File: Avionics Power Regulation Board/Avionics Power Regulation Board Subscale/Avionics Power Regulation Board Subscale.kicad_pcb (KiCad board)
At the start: 2 copper layers, 7 parts, among them J1 282841-2, J2 282841-2, U1 LM2576HVS-5

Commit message: Updated Subscale Board
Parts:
- removed C1: EEUFR1V101B, EEUFR1V101B:CAPPRD350W60D800H1150
- removed C2: EEUTA1V102, EEUTA1V102:CAPPRD750W80D1600H2500
- removed D1: 1N5822, Diode_THT:D_DO-201AD_P15.24mm_Horizontal
- removed L1: RLB9012-101KL, RLB9012-101KL:IND_RLB9012-101KL
- added H1: MountingHole, MountingHole:MountingHole_2.1mm, F.Cu at (120.7, 105.4)
- added H3: MountingHole, MountingHole:MountingHole_2.1mm, F.Cu at (139.7, 54.6)
- added H4: MountingHole, MountingHole:MountingHole_2.1mm, F.Cu at (139.7, 77.5)
- added H5: MountingHole, MountingHole:MountingHole_2.1mm, F.Cu at (163.8, 54.6)
- added H6: MountingHole, MountingHole:MountingHole_2.1mm, F.Cu at (165.1, 77.5)
- added H7: MountingHole, MountingHole:MountingHole_2.1mm, F.Cu at (141.0, 105.4)
- J1: value 282841-2 -> Conn_01x04_Socket; footprint 282841-2:TE_282841-2 -> Connector_PinSocket_2.54mm:PinSocket_1x04_P2.54mm_Vertical
- J2: value 282841-2 -> Conn_01x06_Socket; footprint 282841-2:TE_282841-2 -> Connector_PinSocket_2.54mm:PinSocket_1x06_P2.54mm_Vertical
- U1: value LM2576HVS-5 -> SC0917; footprint Package_TO_SOT_SMD:TO-263-5_TabPin3 -> SC0917:MODULE_SC0917
- moved U1 142.5 mm to (211.6, 69.8), turned to 0 degrees
- moved J2 101.2 mm to (124.5, 118.1), turned to 90 degrees
- moved J1 88.0 mm to (139.7, 62.2), turned to 0 degrees
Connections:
- J1 pad 1: Net-(U1-FB) -> unconnected-(J1-Pin_1-Pad1)
- J1 pad 2: GNDREF -> unconnected-(J1-Pin_2-Pad2)
- J2 pad 1: GNDREF -> unconnected-(J2-Pin_1-Pad1)
- J2 pad 2: Net-(U1-VIN) -> unconnected-(J2-Pin_2-Pad2)
- U1 pad 1: Net-(U1-VIN) -> unconnected-(U1-GP0-Pad1)
- U1 pad 2: Net-(D1-K) -> unconnected-(U1-GP1-Pad2)
- U1 pad 4: Net-(U1-FB) -> unconnected-(U1-GP2-Pad4)
- U1 pad 5: GNDREF -> unconnected-(U1-GP3-Pad5)
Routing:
- net GNDREF: track 108.4 -> 0.00 mm
- net Net-(U1-VIN): track 41.4 -> 0.00 mm
- net Net-(U1-FB): track 40.1 -> 0.00 mm
- net Net-(D1-K): track 25.5 -> 0.00 mm
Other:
- board text added: "BMP 280"

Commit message: Updated Subscale Part 3
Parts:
- moved U1 12.4 mm to (224.0, 68.6)
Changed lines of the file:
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@@
 	(footprint "SC0917:MODULE_SC0917"
 		(layer "F.Cu")
-		(at 211.62 69.85)
+		(at 223.99 68.58)
 		(property "Reference" "U1"
 			(at -8.325 -28.635 0)

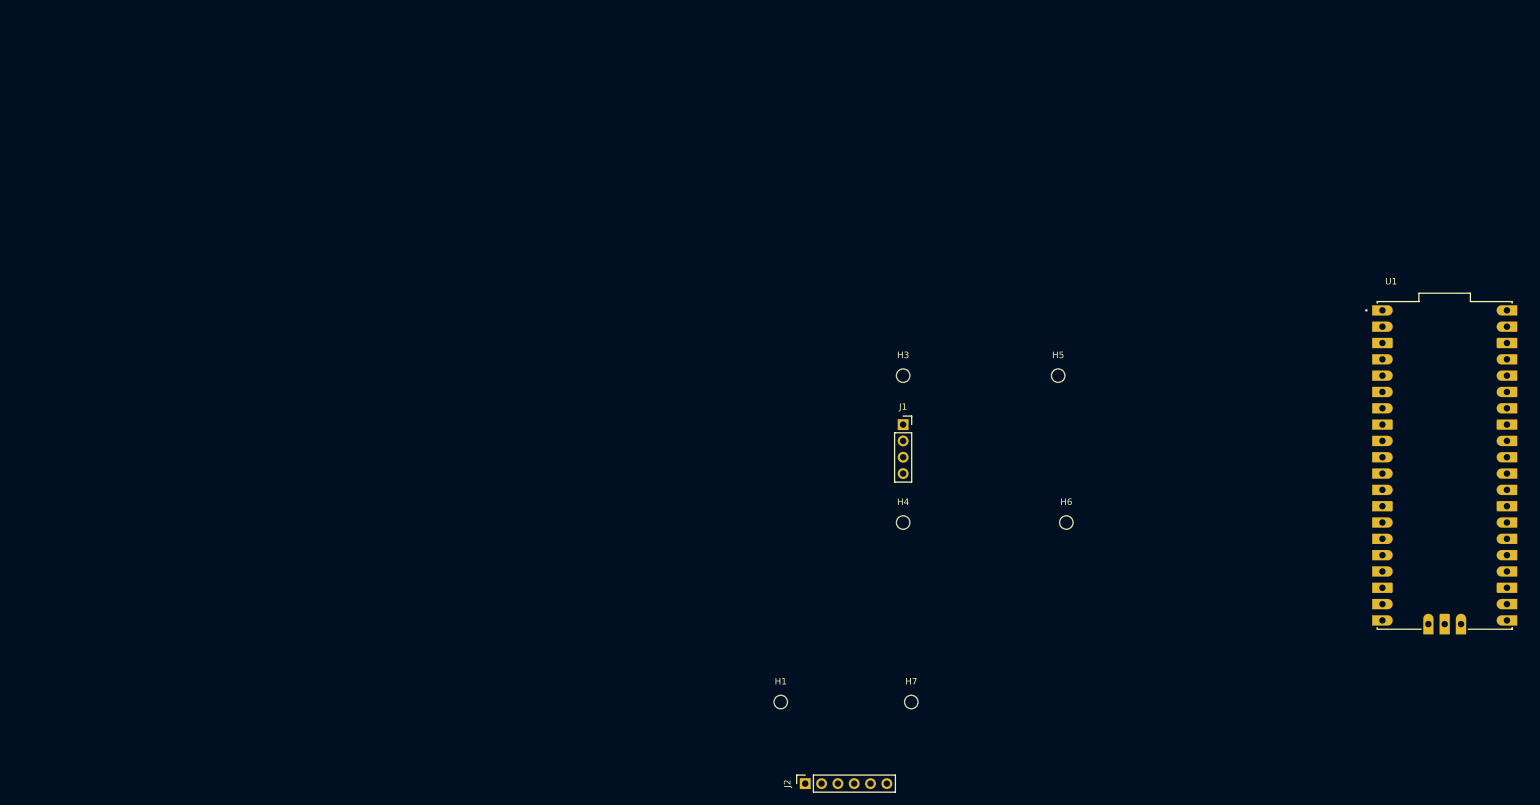
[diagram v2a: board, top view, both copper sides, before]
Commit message: Radio Added
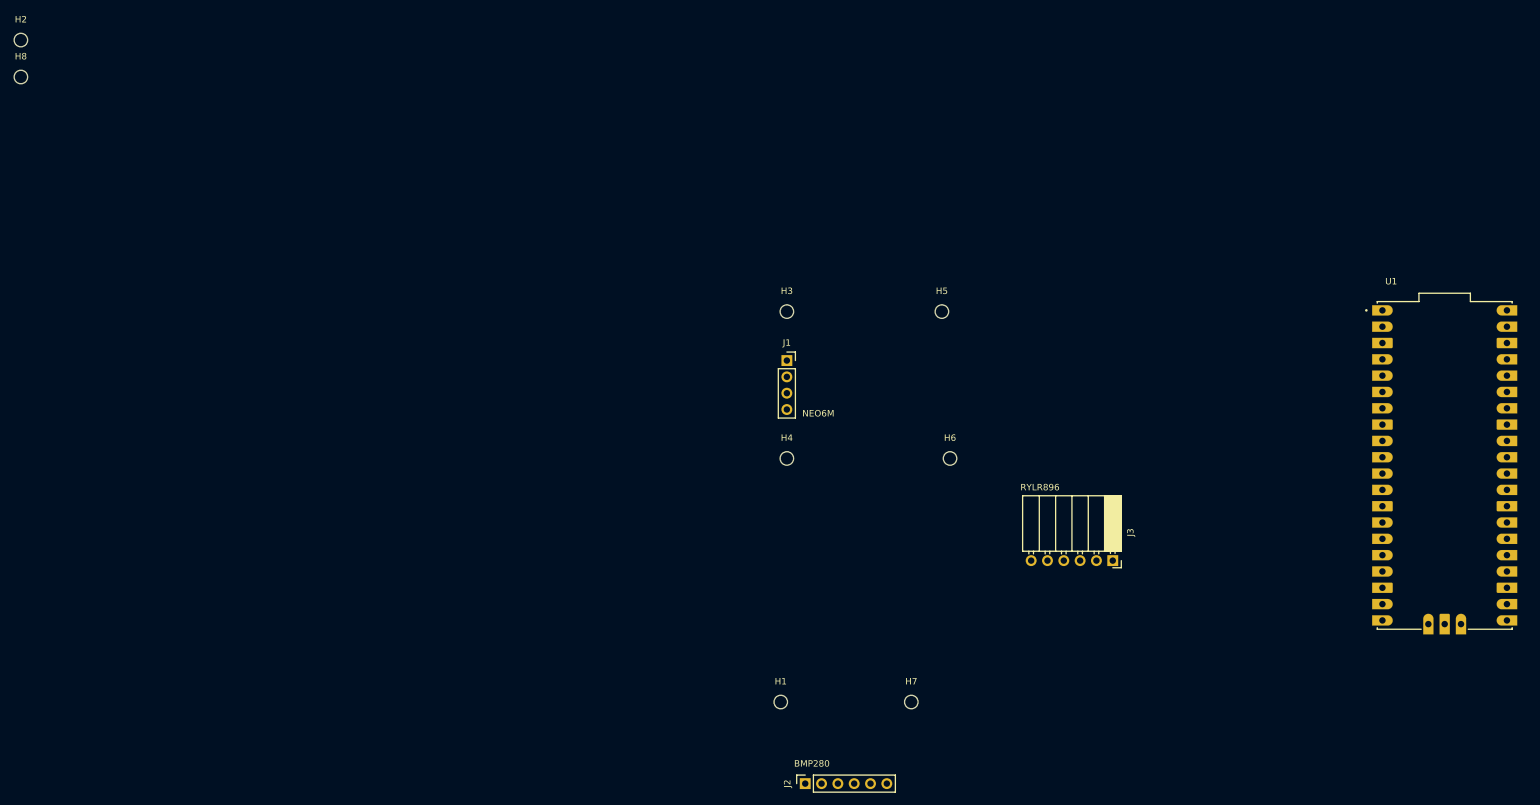
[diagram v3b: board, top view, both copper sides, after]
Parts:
- added H2: MountingHole, MountingHole:MountingHole_2.1mm, F.Cu at (2.38, 2.38)
- added H8: MountingHole, MountingHole:MountingHole_2.1mm, F.Cu at (2.38, 8.12)
- added J3: Conn_01x06_Socket, Connector_PinSocket_2.54mm:PinSocket_1x06_P2.54mm_Horizontal, F.Cu at (172.3, 83.4)
- moved H5 20.7 mm to (145.7, 44.6)
- moved H3 20.7 mm to (121.6, 44.6)
- moved H4 20.7 mm to (121.6, 67.5)
- moved H6 20.7 mm to (147.0, 67.5)
- moved J1 20.7 mm to (121.6, 52.3)

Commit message: Added Accurate footprints
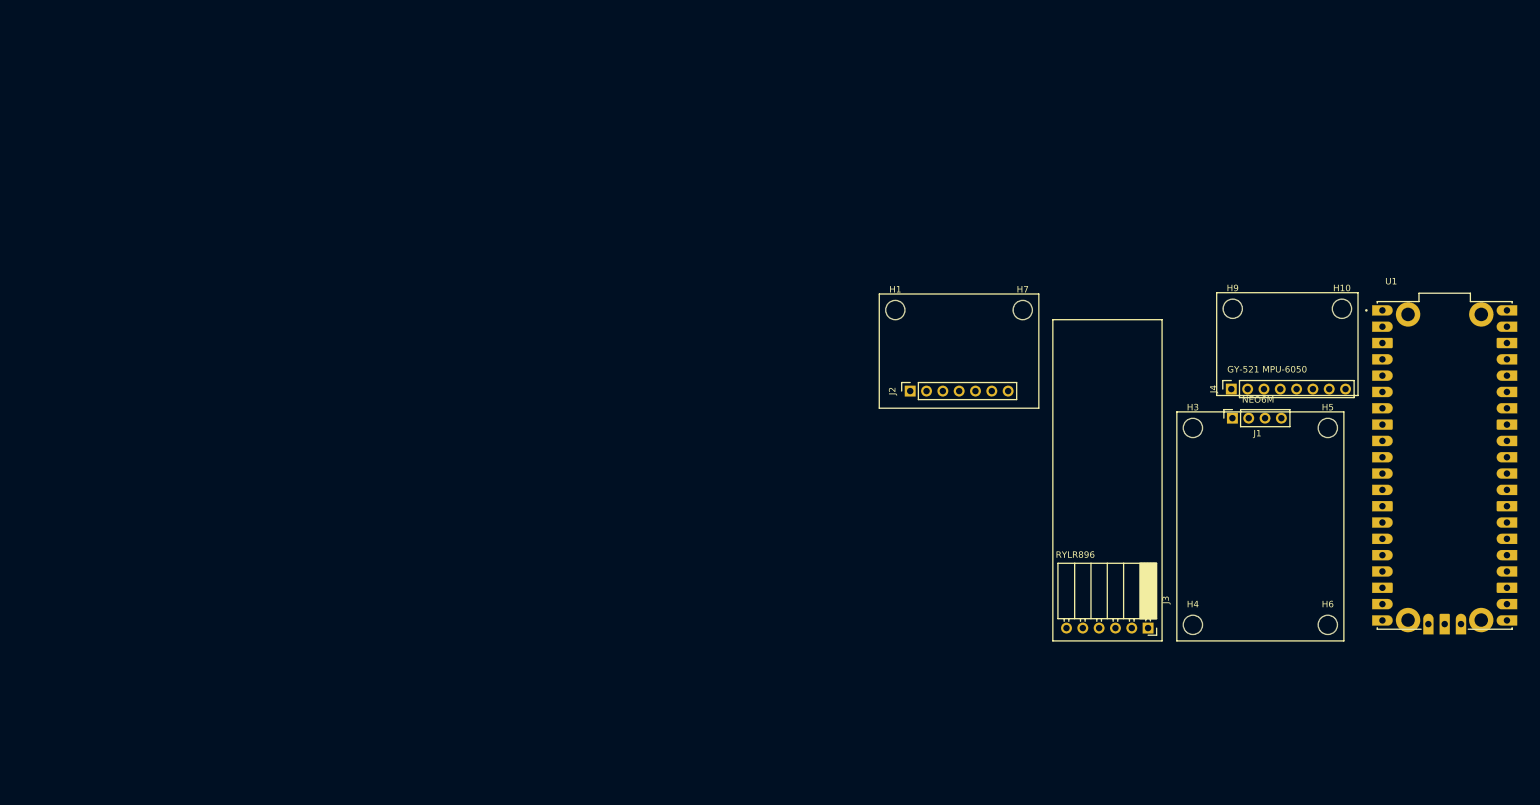
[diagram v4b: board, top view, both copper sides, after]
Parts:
- removed H2, H8: MountingHole, MountingHole:MountingHole_2.1mm
- added H10: MountingHole, MountingHole:MountingHole_2.1mm, F.Cu at (208.0, 44.2)
- added H9: MountingHole, MountingHole:MountingHole_2.1mm, F.Cu at (191.0, 44.2)
- added J4: Conn_01x08_Socket, Connector_PinSocket_2.54mm:PinSocket_1x08_P2.54mm_Vertical, F.Cu at (190.8, 56.7)
- J2: footprint Connector_PinSocket_2.54mm:PinSocket_1x06_P2.54mm_Vertical -> Connector_PinSocket_2.54mm:PinSocket_1x07_P2.54mm_Vertical
- moved J1 69.9 mm to (190.9, 61.2), turned to 90 degrees
- moved H4 68.3 mm to (184.8, 93.4)
- moved H3 65.7 mm to (184.8, 62.8)
- moved H6 64.3 mm to (205.8, 93.4)
- moved H1 63.6 mm to (138.5, 44.4)
- moved H7 63.4 mm to (158.3, 44.4)
- moved J2 63.2 mm to (140.8, 57.0)
- moved H5 62.7 mm to (205.8, 62.8)
- moved J3 11.9 mm to (177.8, 93.9)

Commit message: Test PCB Layout
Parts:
- added G***: LOGO, AIAA Logo:AIAA Logo, F.Cu at (150.5, 86.6)
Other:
- board outline added: 101.8 x 59.5 mm
